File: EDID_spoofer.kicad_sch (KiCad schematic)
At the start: 9 parts, among them J1 DE15_Plug_HighDensity_Mountin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, J2 DE15_Receptacle_HighDensity_M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, J3 Conn_01x04, U1 24LCS22A

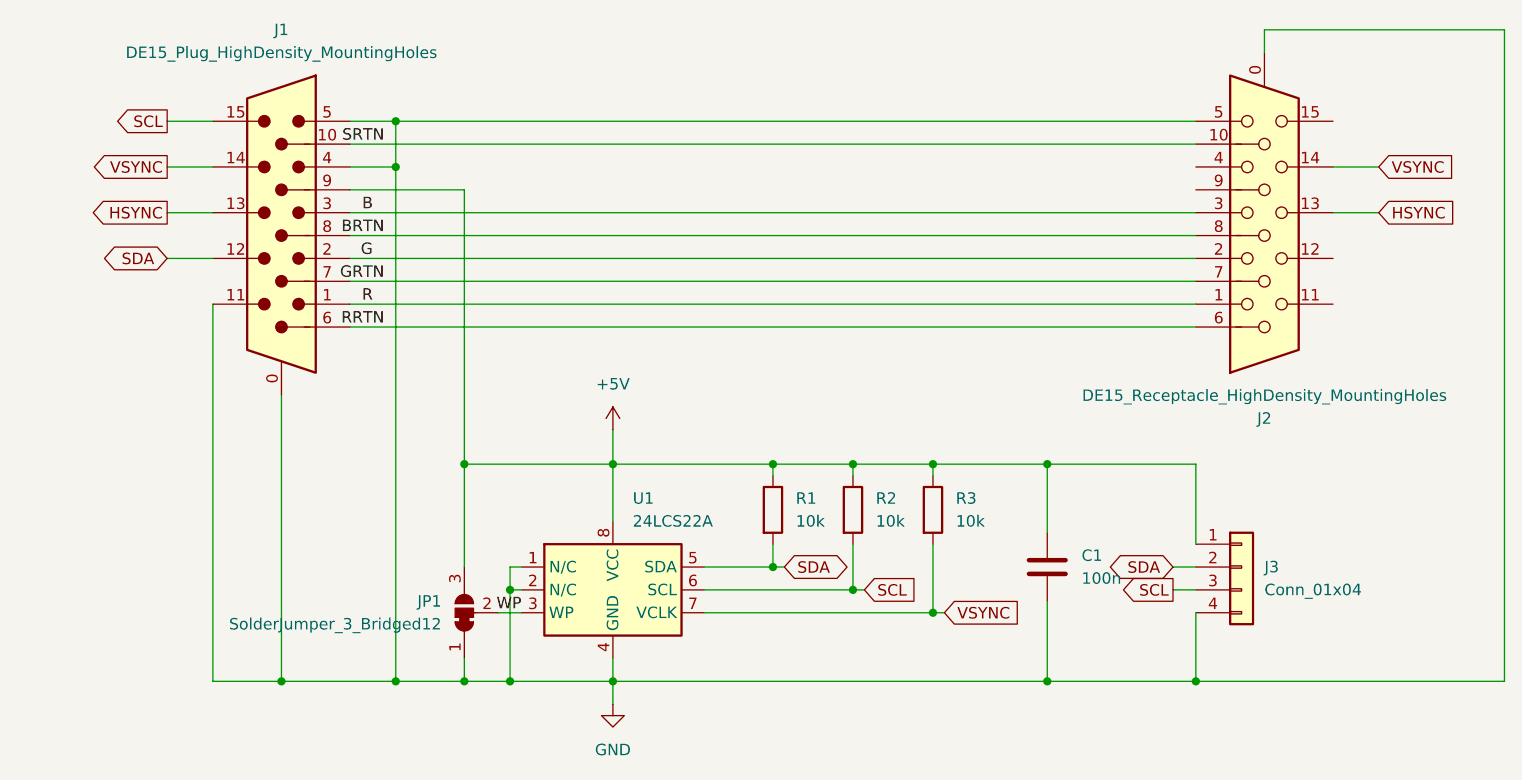
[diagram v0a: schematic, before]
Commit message: Add DDC1 ID0-3 jumpers
Allow configuration of DDC1 monitor ID bits 0-3.
Defaults to ID0 and ID2 grounded, ID1 and ID3 open -
- Color monitor which supports 1024x768.

ID1 and ID3 are shared with SDA and SCL, hence unset by default.

Also layout and signal integrity improvements.
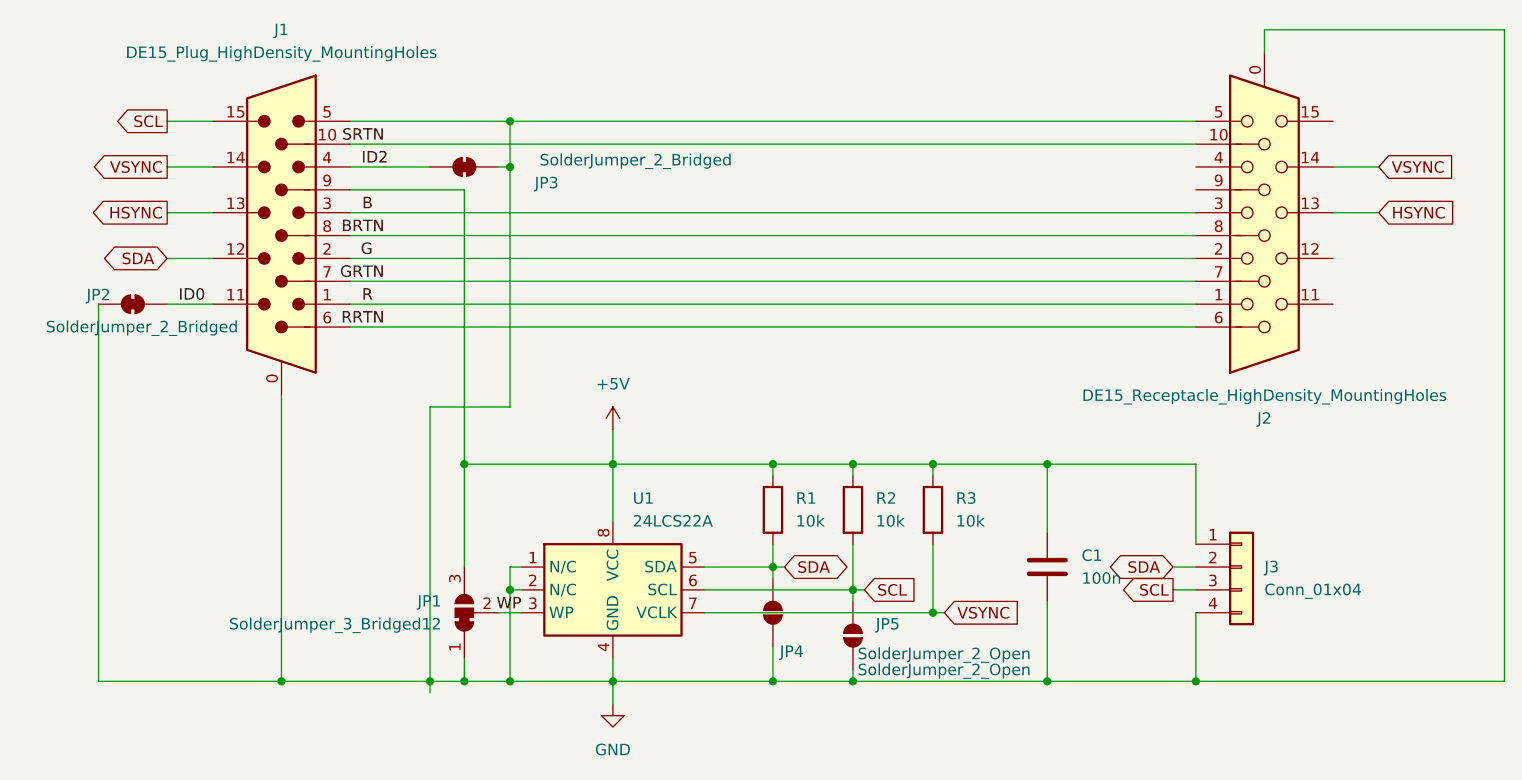
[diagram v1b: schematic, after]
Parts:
- added JP2, JP3: SolderJumper_2_Bridged, Jumper:SolderJumper-2_P1.3mm_Bridged_RoundedPad1.0x1.5mm, symbol Jumper:SolderJumper_2_Bridged
- added JP4, JP5: SolderJumper_2_Open, Jumper:SolderJumper-2_P1.3mm_Open_RoundedPad1.0x1.5mm, symbol Jumper:SolderJumper_2_Open
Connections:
- net GND: now also JP2.1 (A), JP3.1 (A), JP4.1 (A), JP5.1 (A); no longer J1.11, J1.4
- net SCL: now also JP5.2 (B)
- net SDA: now also JP4.2 (B)
- new net ID0: J1.11, JP2.2 (B)
- new net ID2: J1.4, JP3.2 (B)
